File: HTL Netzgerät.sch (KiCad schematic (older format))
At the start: 65 parts, among them J1 0.7/20.32mm, T1 BC547, T2 BC547, T3 BC547, T4 BC547, T5 BC547, T6 BC557, T7 BC557, T8 BC639, X1 AUX1_AC1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

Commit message: Libs und TODOs aktualisiert
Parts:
- C1: footprint v5_Capacitor_THT:CP_Radial_D13.0mm_P5.00mm -> Capacitor_THT:CP_Radial_D13.0mm_P5.00mm; symbol v5_Device:CP -> Device:C_Polarized
- C2, C3: footprint v5_Capacitor_THT:C_Rect_L7.2mm_W4.5mm_P5.00mm_FKS2_FKP2_MKS2_MKP2 -> Capacitor_THT:C_Rect_L7.2mm_W4.5mm_P5.00mm_FKS2_FKP2_MKS2_MKP2; symbol v5_Device:C -> Device:C
- C4, C6: footprint v5_Capacitor_THT:CP_Radial_D8.0mm_P5.00mm -> Capacitor_THT:CP_Radial_D8.0mm_P5.00mm; symbol v5_Device:CP -> Device:C_Polarized
- C5: footprint v5_Capacitor_THT:CP_Axial_L30.0mm_D18.0mm_P35.00mm_Horizontal -> Capacitor_THT:CP_Axial_L30.0mm_D18.0mm_P35.00mm_Horizontal; symbol v5_Device:CP -> Device:C_Polarized
- C_Ext1: footprint v5_Capacitor_THT:C_Rect_L19.0mm_W6.0mm_P15.00mm_MKS4 -> Capacitor_THT:C_Rect_L19.0mm_W6.0mm_P15.00mm_MKS4; symbol t14_passive:C -> Device:C
- D1, D2: footprint v5_Diode_THT:D_A-405_P12.70mm_Horizontal -> Diode_THT:D_A-405_P12.70mm_Horizontal; symbol v5_Device:D_Zener -> Device:D_Zener
- D3, D4, D5, D6: footprint v5_Diode_THT:D_A-405_P12.70mm_Horizontal -> Diode_THT:D_A-405_P12.70mm_Horizontal; symbol v5_Device:D -> Device:D
- D_Ext1: footprint v5_Diode_THT:D_DO-27_P15.24mm_Horizontal -> Diode_THT:D_DO-27_P15.24mm_Horizontal; symbol v5_Device:D_Schottky -> Device:D_Schottky
- GL1, GL2: footprint v5_Diode_THT:Diode_Bridge_Round_D9.0mm -> Diode_THT:Diode_Bridge_Round_D9.0mm; symbol v4_device:D_Bridge_+A-A -> Device:D_Bridge_+A-A
- GL3: footprint v5_Diode_THT:Diode_Bridge_32.0x5.6x17.0mm_P10.0mm_P7.5mm -> Diode_THT:Diode_Bridge_32.0x5.6x17.0mm_P10.0mm_P7.5mm; symbol v4_device:D_Bridge_-AA+ -> Device:D_Bridge_-AA+
- I1, I2, I3: symbol t14_testing:Current -> htl_virtual:ARROW
- J1: footprint v5_Resistor_THT:R_Axial_DIN0516_L15.5mm_D5.0mm_P20.32mm_Horizontal -> Resistor_THT:R_Axial_DIN0516_L15.5mm_D5.0mm_P20.32mm_Horizontal; symbol HTL~Netzgerät:Jumper-Wire -> Device:R
- MK1, MK2, MK3: footprint v5_MountingHole:MountingHole_3mm -> MountingHole:MountingHole_3mm; symbol v4_Mechanical:Mounting_Hole -> Mechanical:MountingHole
- R1, R10, R11, R12, R13, R2, R3, R4, R5, R7, R8, R9: footprint v5_Resistor_THT:R_Axial_DIN0411_L9.9mm_D3.6mm_P12.70mm_Horizontal -> Resistor_THT:R_Axial_DIN0411_L9.9mm_D3.6mm_P12.70mm_Horizontal; symbol v5_Device:R -> Device:R
- R14, R15: footprint v5_Potentiometer_THT:Potentiometer_Piher_PT-15-V02_Vertical -> Potentiometer_THT:Potentiometer_Piher_PT-15-V02_Vertical; symbol v5_Device:R_POT -> Device:R_Potentiometer
- R16, R17: footprint v5_Potentiometer_THT:Potentiometer_Piher_PT-15-H25_Horizontal -> Potentiometer_THT:Potentiometer_Piher_PT-15-H25_Horizontal; symbol v5_Device:R_POT -> Device:R_Potentiometer
- R6: footprint v5_Resistor_THT:R_Axial_DIN0918_L18.0mm_D9.0mm_P22.86mm_Horizontal -> Resistor_THT:R_Axial_DIN0918_L18.0mm_D9.0mm_P22.86mm_Horizontal; symbol v5_Device:R -> Device:R
- T1, T2, T3, T4, T5: symbol v4_Transistor:BC547 -> Transistor_BJT:BC547
- T6, T7: symbol v5_Transistor_BJT:BC557 -> Transistor_BJT:BC557
- T8: symbol v5_Device:Q_NPN_ECB -> Device:Q_NPN_ECB
- T_Ext1: footprint v5_Package_TO_SOT_THT:TO-3 -> Package_TO_SOT_THT:TO-3; symbol v5_Device:Q_NPN_BEC -> Device:Q_NPN_BEC
- X1, X10, X11, X12, X13, X14, X15, X2, X3, X4, X5, X6, X7, X8, X9: footprint v5_TestPoint:TestPoint_THTPad_D2.5mm_Drill1.2mm -> TestPoint:TestPoint_THTPad_D2.5mm_Drill1.2mm; symbol v4_Connector:Conn_01x01 -> Connector_Generic:Conn_01x01

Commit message: Einige Korrekturen eingepflegt für Version 2.1
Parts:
- J1: symbol Device:R -> htl_mechanical:Drahtbruecke
- MK1, MK2, MK3: footprint MountingHole:MountingHole_3mm -> MountingHole:MountingHole_3.2mm_M3
- R14, R15: footprint Potentiometer_THT:Potentiometer_Piher_PT-15-V02_Vertical -> HTL_Netzgeraet:Potentiometer_Piher_PT-15-V02_Vertical
- R6: footprint Resistor_THT:R_Axial_DIN0918_L18.0mm_D9.0mm_P22.86mm_Horizontal -> Resistor_THT:R_Axial_DIN0922_L20.0mm_D9.0mm_P30.48mm_Horizontal
- T1, T2, T3, T4, T5, T6, T7, T8: footprint HTL Netzgerät:TO-92 -> HTL_Netzgeraet:TO-92
- X1, X10, X11, X12, X13, X14, X15, X2, X3, X4, X5, X6, X7, X8, X9: footprint TestPoint:TestPoint_THTPad_D2.5mm_Drill1.2mm -> HTL_Netzgeraet:TestPoint_THTPad_D2.5mm_Drill1.25mm
- renumbered R16 to P1, R17 to P2
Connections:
- wire segments 185 -> 187
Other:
- note added: "10V~~"
- note added: "27V~~"
- note added: "36V~~"
- note added: "Für Transistor T8 wurde bisher (bis V2.0)\nBC141, 2N1613 oder 2N3735\nim TO8-Gehäuse verwendet"
- note added: "Justierprint\nP1+P3 (500R)"
- note added: "Justierprint\nP2+P4 (500R)"
- moved on the sheet: J1, X5, X6

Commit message: Weitere Verbesserungen, Drahtbrücke, Texte, siehe Changelog
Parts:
- C1, C4, C5, C6: symbol Device:C_Polarized -> HTL-Netzgerät-rescue:C_Polarized-Device
- GL3: footprint Diode_THT:Diode_Bridge_32.0x5.6x17.0mm_P10.0mm_P7.5mm -> HTL_Netzgeraet:Brueckengleichrichter_p7.4-7.2-9.5mm
- J1: footprint Resistor_THT:R_Axial_DIN0516_L15.5mm_D5.0mm_P20.32mm_Horizontal -> HTL_Netzgeraet:Drahtbruecke_d0.7mm_P20.32mm
- P1, P2, R14, R15: symbol Device:R_Potentiometer -> HTL-Netzgerät-rescue:R_Potentiometer-Device
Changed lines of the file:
@@
 	3150 2050 3150 1100
 $Comp
-L Device:C_Polarized C6
+L HTL-Netzgerät-rescue:C_Polarized-Device C6
 U 1 1 5DFE9419
 P 3550 1850
@@
 F 0 "GL3" V 1546 2244 50  0000 L CNN
 F 1 "3A" V 1455 2244 50  0000 L CNN
-F 2 "Diode_THT:Diode_Bridge_32.0x5.6x17.0mm_P10.0mm_P7.5mm" H 1500 1900 50  0001 C CNN
+F 2 "HTL_Netzgeraet:Brueckengleichrichter_p7.4-7.2-9.5mm" H 1500 1900 50  0001 C CNN
 F 3 "" H 1500 1900 50  0001 C CNN
 	1    1500 1900
@@
 	1500 1600 1500 950
 $Comp
-L Device:C_Polarized C5
+L HTL-Netzgerät-rescue:C_Polarized-Device C5
 U 1 1 5DFF6855
 P 2050 2650
@@
 	9650 5300 9650 4900
 $Comp
-L Device:C_Polarized C4
+L HTL-Netzgerät-rescue:C_Polarized-Device C4
 U 1 1 5E02FC15
 P 9150 5600
@@
 Connection ~ 6200 5600
 $Comp
-L Device:C_Polarized C1
+L HTL-Netzgerät-rescue:C_Polarized-Device C1
 U 1 1 5E08383F
 P 8850 3550
@@
 	6850 5250 6850 5450
 $Comp
-L Device:R_Potentiometer R15
+L HTL-Netzgerät-rescue:R_Potentiometer-Device R15
 U 1 1 5E0CA8CB
 P 6850 6000
@@
 	6850 5800 6850 5750
 $Comp
-L Device:R_Potentiometer P1
+L HTL-Netzgerät-rescue:R_Potentiometer-Device P1
 U 1 1 5E0CEA26
 P 7400 4950
@@
 	4050 5250 4050 5450
 $Comp
-L Device:R_Potentiometer R14
+L HTL-Netzgerät-rescue:R_Potentiometer-Device R14
 U 1 1 5E10F148
 P 4050 6000
@@
 	4050 5800 4050 5750
 $Comp
-L Device:R_Potentiometer P2
+L HTL-Netzgerät-rescue:R_Potentiometer-Device P2
 U 1 1 5E123D5C
 P 4600 4950
@@
 F 0 "J1" H 3800 4450 50  0000 C CNN
 F 1 "0.7/20.32mm" H 3750 4300 50  0000 C CNN
-F 2 "Resistor_THT:R_Axial_DIN0516_L15.5mm_D5.0mm_P20.32mm_Horizontal" V 3730 4350 50  0001 C CNN
+F 2 "HTL_Netzgeraet:Drahtbruecke_d0.7mm_P20.32mm" V 3730 4350 50  0001 C CNN
 F 3 "~" H 3800 4350 50  0001 C CNN
 	1    3800 4350

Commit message: Fertig zur Produktion, Gerber, Screenshots, Bestückungsdruck, ...
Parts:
- R1, R10, R11, R12, R13, R2, R3, R4, R5, R7, R8, R9: footprint Resistor_THT:R_Axial_DIN0411_L9.9mm_D3.6mm_P12.70mm_Horizontal -> HTL_Netzgeraet:R_Axial_DIN0411_L9.9mm_D3.6mm_P12.70mm_Horizontal
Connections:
- no-connect marks 3 -> 10
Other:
- moved on the sheet: X11
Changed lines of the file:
@@
 Sheet 1 1
 Title "HTL-Netzgerät - Hauptplatine"
-Date "2020-11-16"
+Date "2020-11-19"
 Rev "V2.1"
-Comp "HTL-Steyr"
+Comp "HTL Steyr"
 Comment1 "überarbeitet von Karl Zeilhofer"
 Comment2 ""
@@
 F 0 "R9" H 4070 1346 50  0000 L CNN
 F 1 "27k" H 4070 1255 50  0000 L CNN
-F 2 "Resistor_THT:R_Axial_DIN0411_L9.9mm_D3.6mm_P12.70mm_Horizontal" V 3930 1300 50  0001 C CNN
+F 2 "HTL_Netzgeraet:R_Axial_DIN0411_L9.9mm_D3.6mm_P12.70mm_Horizontal" V 3930 1300 50  0001 C CNN
 F 3 "~" H 4000 1300 50  0001 C CNN
 	1    4000 1300
@@
 F 0 "R13" H 7230 1954 50  0000 R CNN
 F 1 "27k" H 7230 2045 50  0000 R CNN
-F 2 "Resistor_THT:R_Axial_DIN0411_L9.9mm_D3.6mm_P12.70mm_Horizontal" V 7230 2000 50  0001 C CNN
+F 2 "HTL_Netzgeraet:R_Axial_DIN0411_L9.9mm_D3.6mm_P12.70mm_Horizontal" V 7230 2000 50  0001 C CNN
 F 3 "~" H 7300 2000 50  0001 C CNN
 	1    7300 2000
@@
 F 0 "R11" H 7680 2454 50  0000 R CNN
 F 1 "10k" H 7680 2545 50  0000 R CNN
-F 2 "Resistor_THT:R_Axial_DIN0411_L9.9mm_D3.6mm_P12.70mm_Horizontal" V 7680 2500 50  0001 C CNN
+F 2 "HTL_Netzgeraet:R_Axial_DIN0411_L9.9mm_D3.6mm_P12.70mm_Horizontal" V 7680 2500 50  0001 C CNN
 F 3 "~" H 7750 2500 50  0001 C CNN
 	1    7750 2500
@@
 L Connector_Generic:Conn_01x01 X11
 U 1 1 5E00013E
-P 8850 2550
-F 0 "X11" V 8768 2462 50  0000 R CNN
-F 1 "E" V 8723 2462 50  0001 R CNN
-F 2 "HTL_Netzgeraet:TestPoint_THTPad_D2.5mm_Drill1.25mm" H 8850 2550 50  0001 C CNN
-F 3 "~" H 8850 2550 50  0001 C CNN
-	1    8850 2550
+P 8850 2600
+F 0 "X11" V 8768 2512 50  0000 R CNN
+F 1 "E" V 8723 2512 50  0001 R CNN
+F 2 "HTL_Netzgeraet:TestPoint_THTPad_D2.5mm_Drill1.25mm" H 8850 2600 50  0001 C CNN
+F 3 "~" H 8850 2600 50  0001 C CNN
+	1    8850 2600
 	0    -1   -1   0
 $EndComp
@@
 F 0 "R10" H 6130 2004 50  0000 R CNN
 F 1 "220k" H 6130 2095 50  0000 R CNN
-F 2 "Resistor_THT:R_Axial_DIN0411_L9.9mm_D3.6mm_P12.70mm_Horizontal" V 6130 2050 50  0001 C CNN
+F 2 "HTL_Netzgeraet:R_Axial_DIN0411_L9.9mm_D3.6mm_P12.70mm_Horizontal" V 6130 2050 50  0001 C CNN
 F 3 "~" H 6200 2050 50  0001 C CNN
 	1    6200 2050
@@
 F 0 "R12" H 3930 1904 50  0000 R CNN
 F 1 "220k" H 3930 1995 50  0000 R CNN
-F 2 "Resistor_THT:R_Axial_DIN0411_L9.9mm_D3.6mm_P12.70mm_Horizontal" V 3930 1950 50  0001 C CNN
+F 2 "HTL_Netzgeraet:R_Axial_DIN0411_L9.9mm_D3.6mm_P12.70mm_Horizontal" V 3930 1950 50  0001 C CNN
 F 3 "~" H 4000 1950 50  0001 C CNN
 	1    4000 1950
@@
 Connection ~ 6200 1650
 Wire Wire Line
-	8850 2750 8850 2850
+	8850 2800 8850 2850
 Wire Wire Line
 	7750 2650 7750 2850
@@
 F 0 "R8" H 8730 5204 50  0000 R CNN
 F 1 "10k" H 8730 5295 50  0000 R CNN
-F 2 "Resistor_THT:R_Axial_DIN0411_L9.9mm_D3.6mm_P12.70mm_Horizontal" V 8730 5250 50  0001 C CNN
+F 2 "HTL_Netzgeraet:R_Axial_DIN0411_L9.9mm_D3.6mm_P12.70mm_Horizontal" V 8730 5250 50  0001 C CNN
 F 3 "~" H 8800 5250 50  0001 C CNN
 	1    8800 5250
@@
 F 0 "R7" H 8330 5954 50  0000 R CNN
 F 1 "1k" H 8330 6045 50  0000 R CNN
-F 2 "Resistor_THT:R_Axial_DIN0411_L9.9mm_D3.6mm_P12.70mm_Horizontal" V 8330 6000 50  0001 C CNN
+F 2 "HTL_Netzgeraet:R_Axial_DIN0411_L9.9mm_D3.6mm_P12.70mm_Horizontal" V 8330 6000 50  0001 C CNN
 F 3 "~" H 8400 6000 50  0001 C CNN
 	1    8400 6000
@@
 F 0 "R3" H 5780 5804 50  0000 R CNN
 F 1 "330k" H 5780 5895 50  0000 R CNN
-F 2 "Resistor_THT:R_Axial_DIN0411_L9.9mm_D3.6mm_P12.70mm_Horizontal" V 5780 5850 50  0001 C CNN
+F 2 "HTL_Netzgeraet:R_Axial_DIN0411_L9.9mm_D3.6mm_P12.70mm_Horizontal" V 5780 5850 50  0001 C CNN
 F 3 "~" H 5850 5850 50  0001 C CNN
 	1    5850 5850
@@
 F 0 "R1" H 8380 3504 50  0000 R CNN
 F 1 "2k2" H 8380 3595 50  0000 R CNN
-F 2 "Resistor_THT:R_Axial_DIN0411_L9.9mm_D3.6mm_P12.70mm_Horizontal" V 8380 3550 50  0001 C CNN
+F 2 "HTL_Netzgeraet:R_Axial_DIN0411_L9.9mm_D3.6mm_P12.70mm_Horizontal" V 8380 3550 50  0001 C CNN
 F 3 "~" H 8450 3550 50  0001 C CNN
 	1    8450 3550
@@
 F 0 "R2" H 6780 5554 50  0000 R CNN
 F 1 "47k" H 6780 5645 50  0000 R CNN
-F 2 "Resistor_THT:R_Axial_DIN0411_L9.9mm_D3.6mm_P12.70mm_Horizontal" V 6780 5600 50  0001 C CNN
+F 2 "HTL_Netzgeraet:R_Axial_DIN0411_L9.9mm_D3.6mm_P12.70mm_Horizontal" V 6780 5600 50  0001 C CNN
 F 3 "~" H 6850 5600 50  0001 C CNN
 	1    6850 5600
@@
 F 0 "R5" H 2980 5804 50  0000 R CNN
 F 1 "330k" H 2980 5895 50  0000 R CNN
-F 2 "Resistor_THT:R_Axial_DIN0411_L9.9mm_D3.6mm_P12.70mm_Horizontal" V 2980 5850 50  0001 C CNN
+F 2 "HTL_Netzgeraet:R_Axial_DIN0411_L9.9mm_D3.6mm_P12.70mm_Horizontal" V 2980 5850 50  0001 C CNN
 F 3 "~" H 3050 5850 50  0001 C CNN
 	1    3050 5850
@@
 F 0 "R4" H 3980 5554 50  0000 R CNN
 F 1 "120k" H 3980 5645 50  0000 R CNN
-F 2 "Resistor_THT:R_Axial_DIN0411_L9.9mm_D3.6mm_P12.70mm_Horizontal" V 3980 5600 50  0001 C CNN
+F 2 "HTL_Netzgeraet:R_Axial_DIN0411_L9.9mm_D3.6mm_P12.70mm_Horizontal" V 3980 5600 50  0001 C CNN
 F 3 "~" H 4050 5600 50  0001 C CNN
 	1    4050 5600
@@
 Wire Wire Line
 	5050 4200 5050 4350
+NoConn ~ 7200 4650
+NoConn ~ 7200 4950
+NoConn ~ 4400 4650
+NoConn ~ 4400 4950
+NoConn ~ 8550 2250
+NoConn ~ 8850 2050
+NoConn ~ 8850 2450
 $EndSCHEMATC

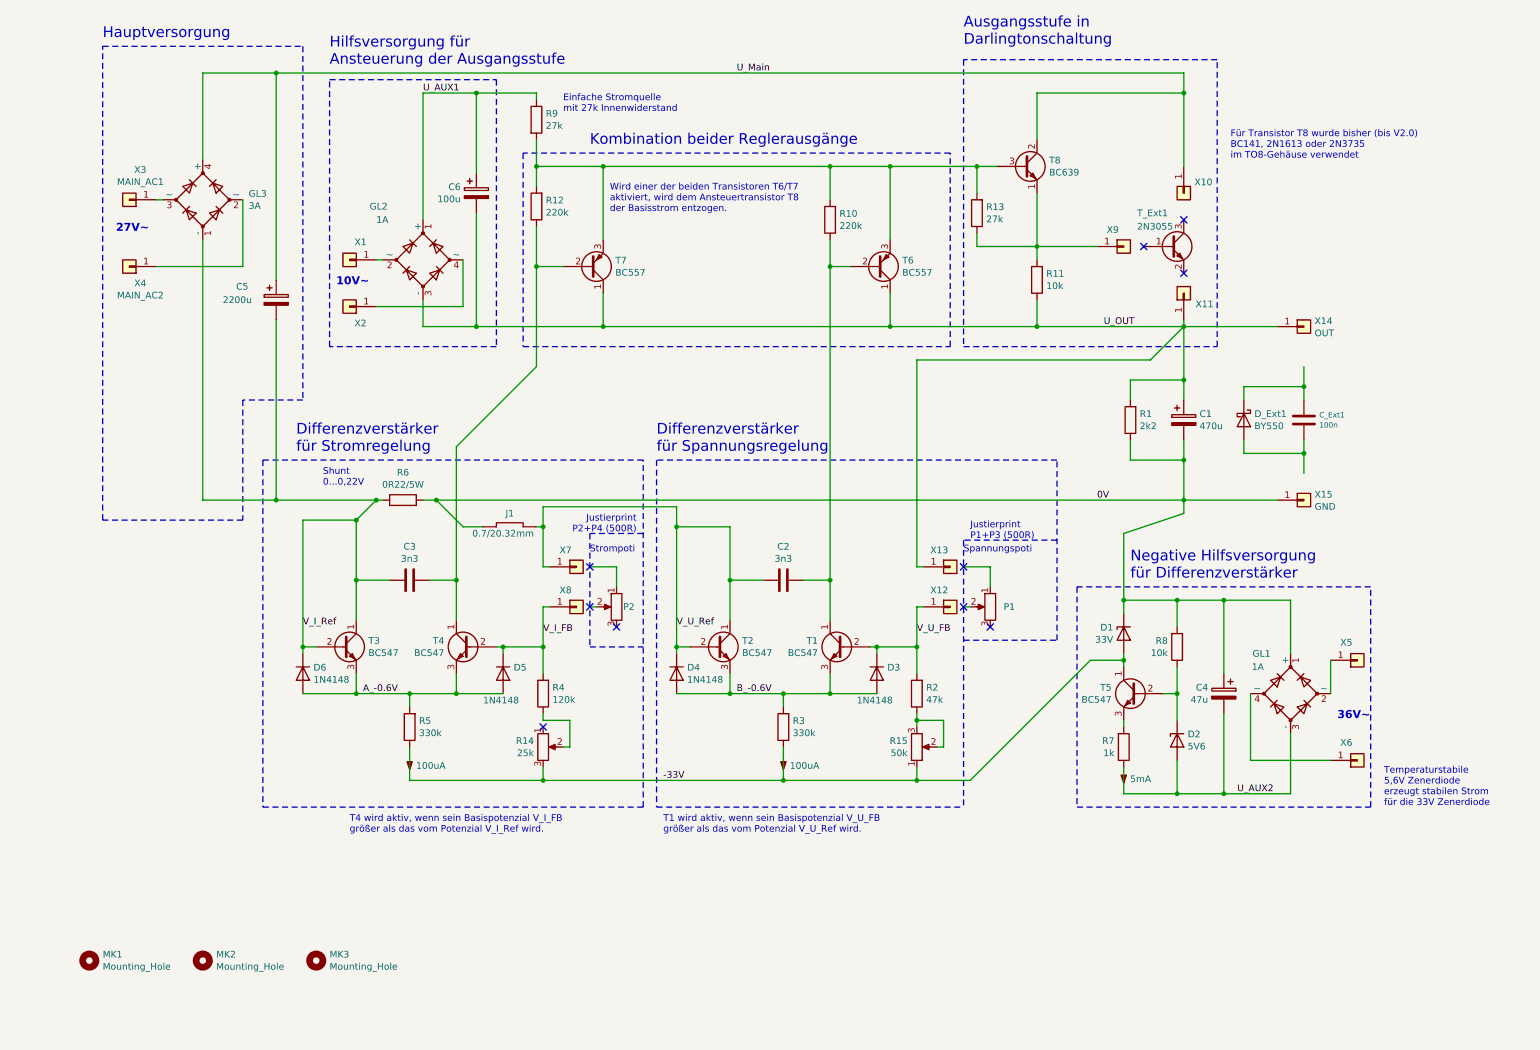
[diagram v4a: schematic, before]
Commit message: v2.2 fertig, 3 Stk. bestellt (einseitig)
siehe CHANGELOG und Github Issues
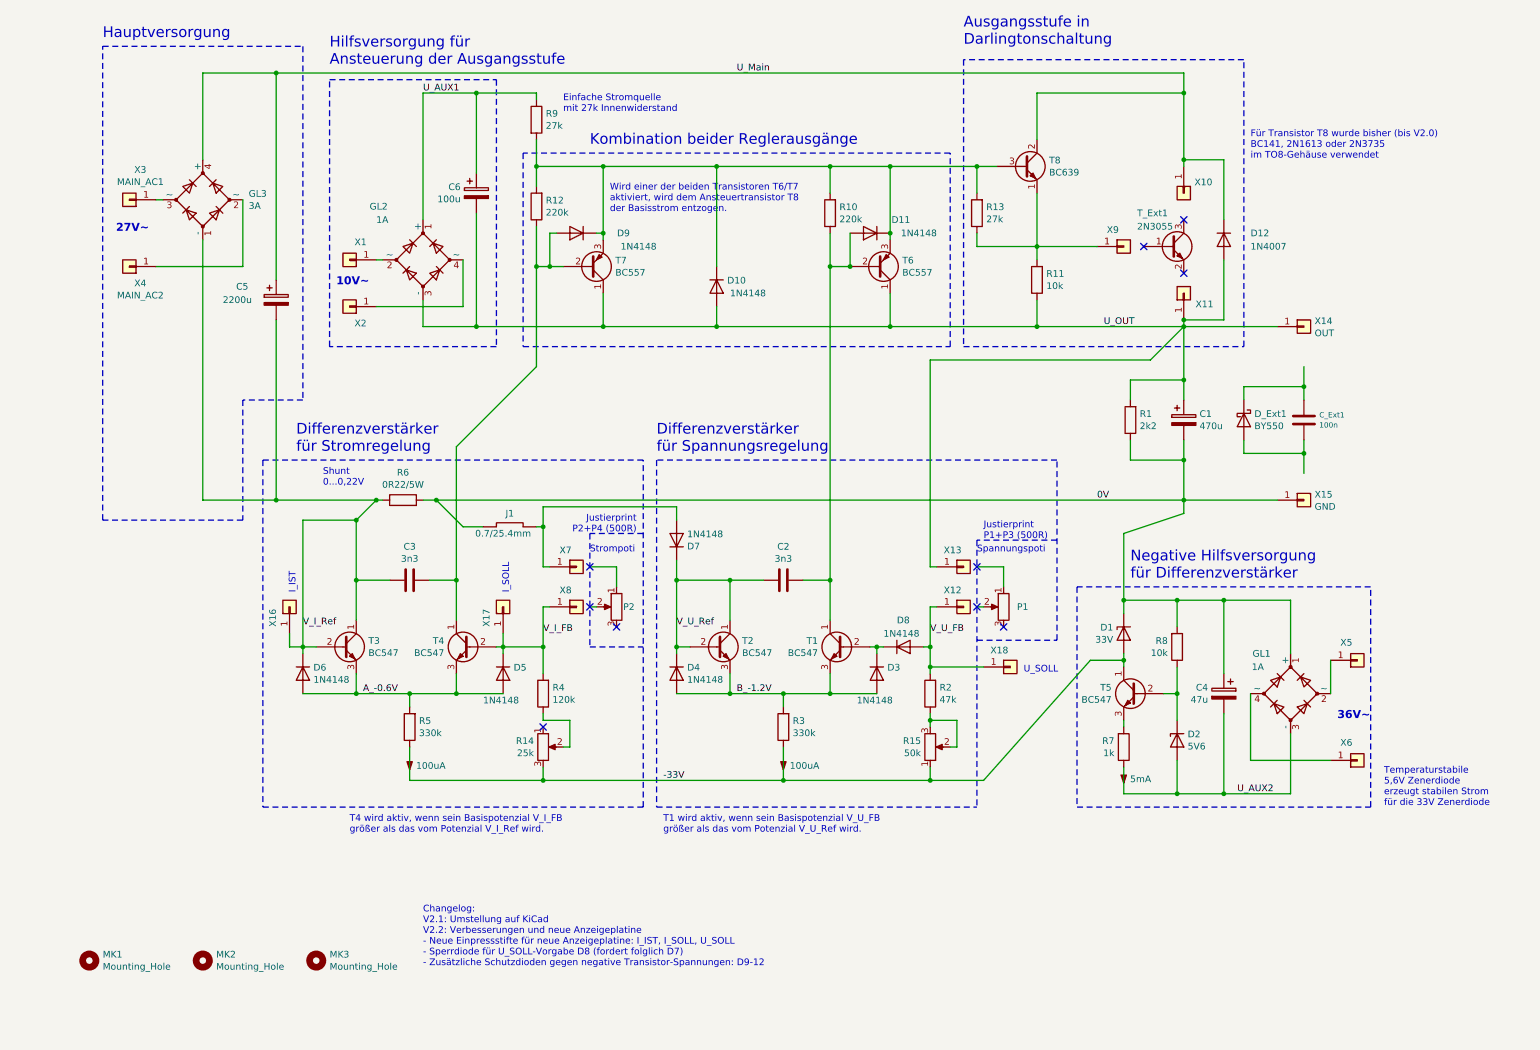
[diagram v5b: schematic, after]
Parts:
- added D10, D11, D7, D9: 1N4148, HTL_Netzgeraet:D_DO-35_SOD27_P12.70mm_Horizontal, symbol Device:D
- added D12: 1N4007, HTL_Netzgeraet:D_DO-41_SOD81_P10.16mm_Horizontal, symbol Device:D
- added D8: 1N4148, HTL_Netzgeraet:D_DO-35_SOD27_P3.81mm_Vertical_KathodeUp, symbol Device:D
- added X16, X17, X18: IPOT+, HTL_Netzgeraet:Einpress-Stift_Drill1.25mm, symbol Connector_Generic:Conn_01x01
- C2, C3: footprint Capacitor_THT:C_Rect_L7.2mm_W4.5mm_P5.00mm_FKS2_FKP2_MKS2_MKP2 -> HTL_Netzgeraet:C_Rect_L7.2mm_W4.5mm_P5.00mm_FKS2_FKP2_MKS2_MKP2
- C4, C6: footprint Capacitor_THT:CP_Radial_D8.0mm_P5.00mm -> HTL_Netzgeraet:CP_Radial_D8.0mm_P5.00mm
- C5: footprint Capacitor_THT:CP_Axial_L30.0mm_D18.0mm_P35.00mm_Horizontal -> HTL_Netzgeraet:CP_Axial_L30.0mm_D18.0mm_P35.00mm_Horizontal
- D1, D2, D5, D6: footprint Diode_THT:D_A-405_P12.70mm_Horizontal -> HTL_Netzgeraet:D_DO-35_SOD27_P12.70mm_Horizontal
- D3, D4: footprint Diode_THT:D_A-405_P12.70mm_Horizontal -> HTL_Netzgeraet:D_DO-35_SOD27_P3.81mm_Vertical_KathodeUp
- GL1, GL2: footprint Diode_THT:Diode_Bridge_Round_D9.0mm -> HTL_Netzgeraet:Diode_Bridge_Round_D9.0mm
- J1: value 0.7/20.32mm -> 0.7/25.4mm
- R6: footprint Resistor_THT:R_Axial_DIN0922_L20.0mm_D9.0mm_P30.48mm_Horizontal -> HTL_Netzgeraet:R_Axial_DIN0922_L20.0mm_D9.0mm_P30.48mm_Horizontal
- X1, X10, X11, X12, X13, X14, X15, X2, X3, X4, X5, X6, X7, X8, X9: footprint HTL_Netzgeraet:TestPoint_THTPad_D2.5mm_Drill1.25mm -> HTL_Netzgeraet:Einpress-Stift_Drill1.25mm
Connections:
- net U_Main: now also D12.1 (K)
- net U_OUT: now also D10.2 (A), D12.2 (A)
- net V_I_FB: now also X17.1 (Pin_1)
- net V_I_Ref: now also X16.1 (Pin_1)
- net V_U_FB: now also D8.2 (A), X18.1 (Pin_1); no longer D3.1 (K), T1.2 (B)
- net V_U_Ref: now also D7.1 (K); no longer J1.2 (B), X7.1 (Pin_1)
- net at R10.2, R12.2, R13.2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: now also D10.1 (K), D11.1 (K), D9.1 (K)
- net at C3.1, R12.1, T4.1 (C)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: now also D9.2 (A)
- net at C2.1, R10.1, T1.1 (C)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: now also D11.2 (A)
- net B_-0.6V renamed B_-1.2V
- new net: D3.1 (K), D8.1 (K), T1.2 (B)
- new net: D7.2 (A), J1.2 (B), X7.1 (Pin_1)
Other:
- note added: "Changelog:\nV2.1: Umstellung auf KiCad\nV2.2: Verbesserungen und neue Anzeigeplatine\n- Neue Einpressstifte für neue Anzeigeplatine: I_IST, I_SOLL, U_SOLL\n- Sperrdiode für U_SOLL-Vorgabe D8 (fordert folglich D7)\n- Zusätzliche Schutzdioden gegen negative Transistor-Spannungen: D9-12\n"
- note added: "I_IST"
- note added: "I_SOLL"
- note added: "U_SOLL"
- moved on the sheet: P1, R10, R15, R2, X12, X13
